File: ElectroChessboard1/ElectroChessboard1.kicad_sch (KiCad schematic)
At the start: 18 parts, among them IC75 DS1307Z+T&R, J2 Conn_01x04_Pin, J3 Conn_01x06, J4 Conn_01x06, SW1 SW_Push, SW2 SW_Push, SW3 SW_Push, SW4 SW_Push, U1 ATmega2560-16A, Y1 Crystal, Y2 XO57CRECNA16M

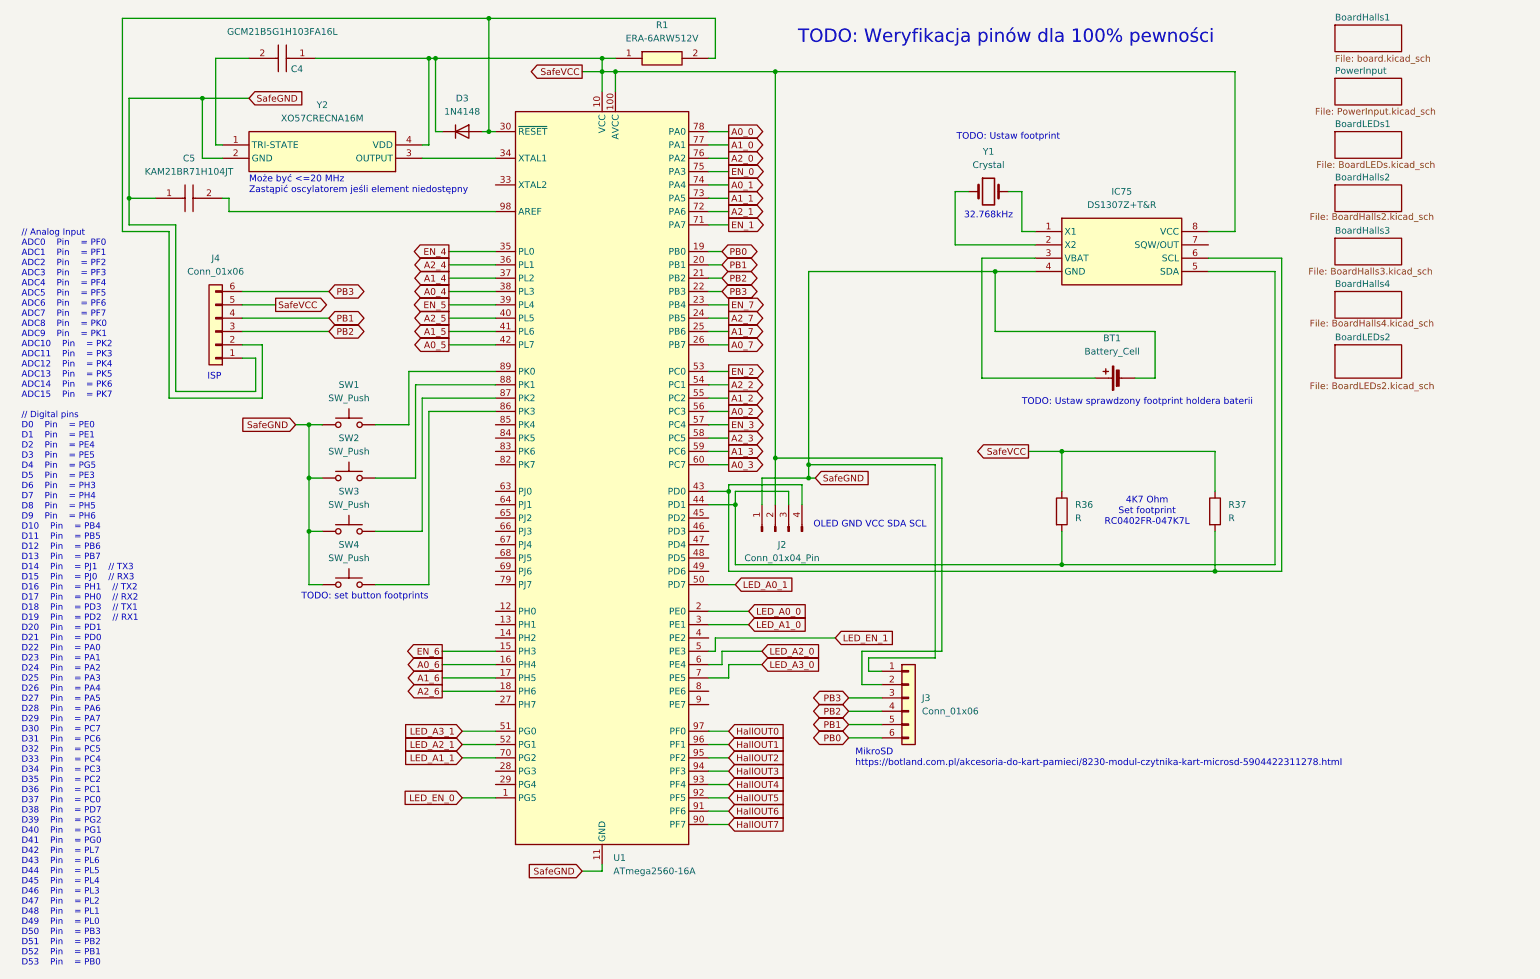
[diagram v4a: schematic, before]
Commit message: Corrected footprints 1
Chosen footprints for JLCPCB
I may add USB insterface chip
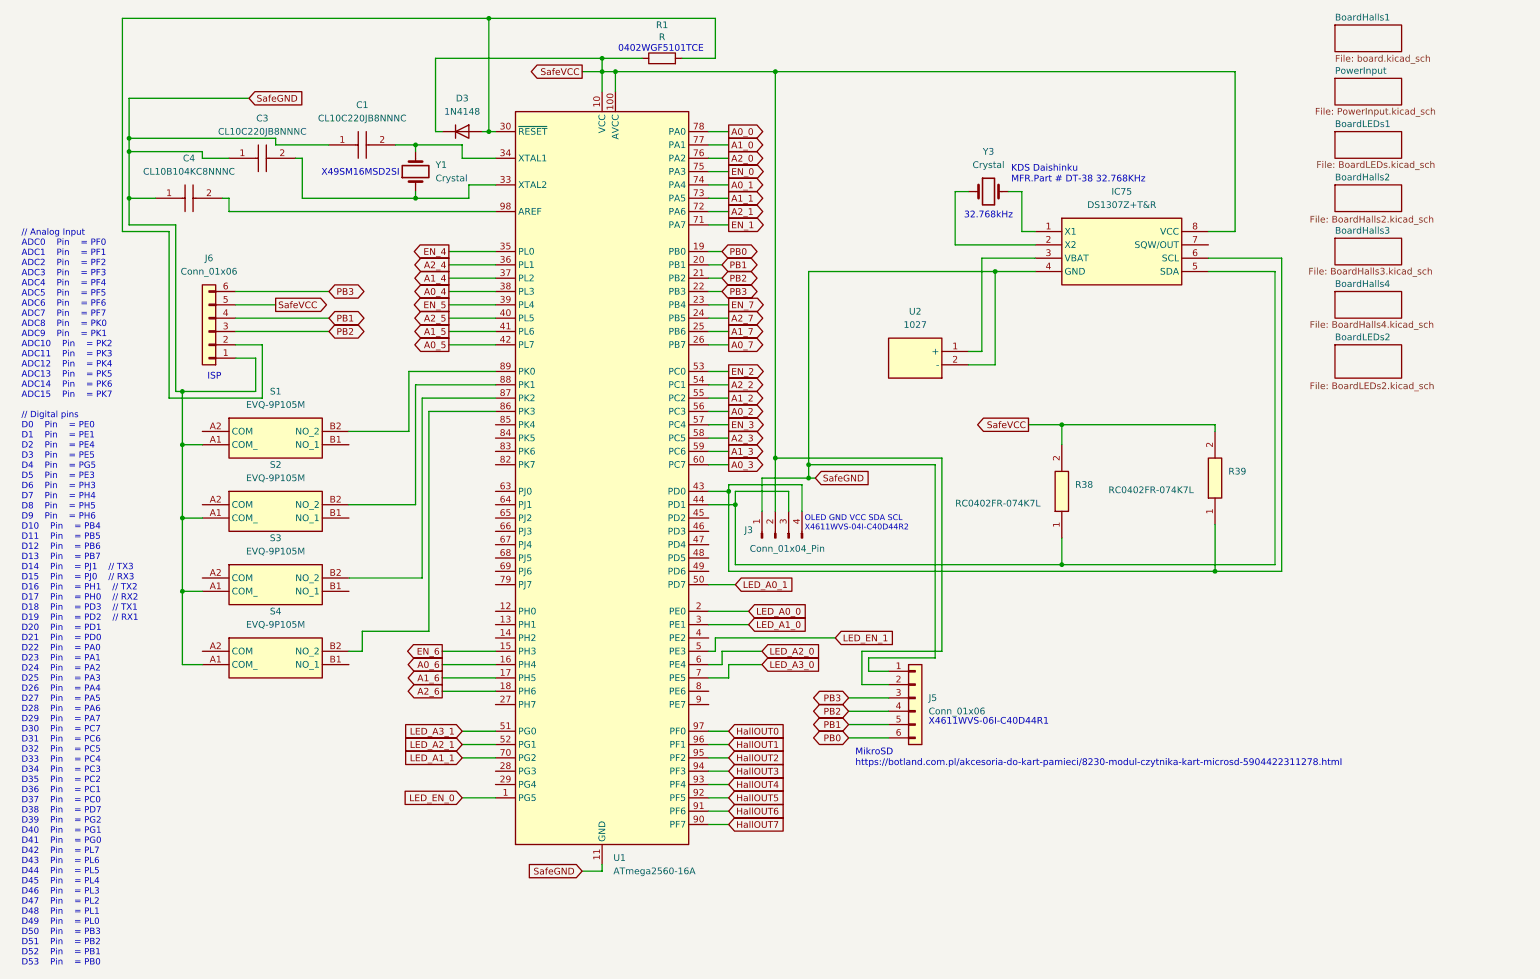
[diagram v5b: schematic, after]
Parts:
- removed BT1: Battery_Cell, symbol Device:Battery_Cell
- removed C4: GCM21B5G1H103FA16L, GCM21, symbol SamacSys_Parts:GCM21B5G1H103FA16L
- removed C5: KAM21BR71H104JT, CAPC2012X94N, symbol SamacSys_Parts:KAM21BR71H104JT
- removed J2: Conn_01x04_Pin, Connector_PinHeader_1.00mm:PinHeader_1x04_P1.00mm_Vertical, symbol Connector:Conn_01x04_Pin
- removed J3, J4: Conn_01x06, Connector_Harwin:Harwin_M20-89006xx_1x06_P2.54mm_Horizontal, symbol Connector_Generic:Conn_01x06
- removed R1: ERA-6ARW512V, ERA6AEB101V, symbol SamacSys_Parts:ERA-6ARW512V
- removed R36, R37: R, symbol Device:R
- removed SW1, SW2, SW3, SW4: SW_Push, symbol Switch:SW_Push
- removed Y2: XO57CRECNA16M, XO57CRECNA16M, symbol SamacSys_Parts:XO57CRECNA16M
- added C1, C3: CL10C220JB8NNNC, SamacSys_Parts:CAPC1608X90N, symbol SamacSys_Parts:CL10C220JB8NNNC
- added C4: CL10B104KC8NNNC, SamacSys_Parts:CAPC1608X90N, symbol SamacSys_Parts:CL10B104KC8NNNC
- added J3: Conn_01x04_Pin, Connector_PinSocket_1.00mm:PinSocket_1x04_P1.00mm_Vertical_SMD_Pin1Left, symbol Connector:Conn_01x04_Pin
- added J5, J6: Conn_01x06, Connector_PinSocket_1.00mm:PinSocket_1x06_P1.00mm_Vertical_SMD_Pin1Right, symbol Connector_Generic:Conn_01x06
- added R1: R, Resistor_SMD:R_0402_1005Metric, symbol Device:R
- added R38, R39: RC0402FR-074K7L, SamacSys_Parts:RESC1005X40N, symbol SamacSys_Parts:RC0402FR-074K7L
- added S1, S2, S3, S4: EVQ-9P105M, SamacSys_Parts:EVQ9P105M, symbol SamacSys_Parts:EVQ-9P105M
- added U2: 1027, SamacSys_Parts:1027, symbol SamacSys_Parts:1027
- added Y3: Crystal, Crystal:Crystal_C38-LF_D3.0mm_L8.0mm_Vertical, symbol Device:Crystal
- D3: footprint Diode_THT:D_DO-35_SOD27_P7.62mm_Horizontal -> Diode_SMD:D_SOD-123
- IC75: footprint SOIC127P600X175-8N -> SamacSys_Parts:SOIC127P600X175-8N
- Y1: footprint (none) -> Crystal:Crystal_SMD_HC49-SD
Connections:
- net PB0: now also J5.6 (Pin_6)
- net PB1: now also J5.5 (Pin_5), J6.4 (Pin_4)
- net PB2: now also J5.4 (Pin_4), J6.3 (Pin_3)
- net PB3: now also J5.3 (Pin_3), J6.6 (Pin_6)
- net SafeGND: now also C1.1, C3.1, C4.1, J3.1 (Pin_1), J5.1 (Pin_1), J6.1 (Pin_1), S1.A1 (COM_), S2.A1 (COM_), S3.A1 (COM_), S4.A1 (COM_), U2.2 (-)
- net SafeVCC: now also J3.2 (Pin_2), J5.2 (Pin_2), J6.5 (Pin_5), R1.1, R38.2, R39.2
- net at IC75.5 (SDA), U1.44 (PD1): now also J3.3 (Pin_3), R38.1
- net at IC75.6 (SCL), U1.43 (PD0): now also J3.4 (Pin_4), R39.1
- net at D3.2 (A), U1.30 (~{RESET}): now also J6.2 (Pin_2), R1.2
- net at U1.33 (XTAL2): now also Y1.1, C3.2
- net at U1.34 (XTAL1): now also Y1.2, C1.2
- net at U1.86 (PK3): now also S4.B2 (NO_2)
- net at U1.87 (PK2): now also S3.B2 (NO_2)
- net at U1.88 (PK1): now also S2.B2 (NO_2)
- net at U1.89 (PK0): now also S1.B2 (NO_2)
- net at U1.98 (AREF): now also C4.2
- net at IC75.1 (X1): now also Y3.2; no longer Y1.2
- net at IC75.2 (X2): now also Y3.1; no longer Y1.1
- net at IC75.3 (VBAT): now also U2.1 (+)
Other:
- note added: "0402WGF5101TCE"
- note added: "KDS Daishinku MFR.Part # DT-38 32.768KHz"
- note added: "OLED GND VCC SDA SCL X4611WVS-04I-C40D44R2"
- note added: "X4611WVS-06I-C40D44R1"
- note added: "X49SM16MSD2SI"
- note removed: "4K7 Ohm Set footprint RC0402FR-047K7L"
- note removed: "Może być <=20 MHz Zastąpić oscylatorem jeśli element niedostępny"
- note removed: "OLED GND VCC SDA SCL"
- note removed: "TODO: Ustaw footprint"
- note removed: "TODO: Ustaw sprawdzony footprint holdera baterii"
- note removed: "TODO: Weryfikacja pinów dla 100% pewności"
- note removed: "TODO: set button footprints"

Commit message: Added FT232RL
Ready for PCB design
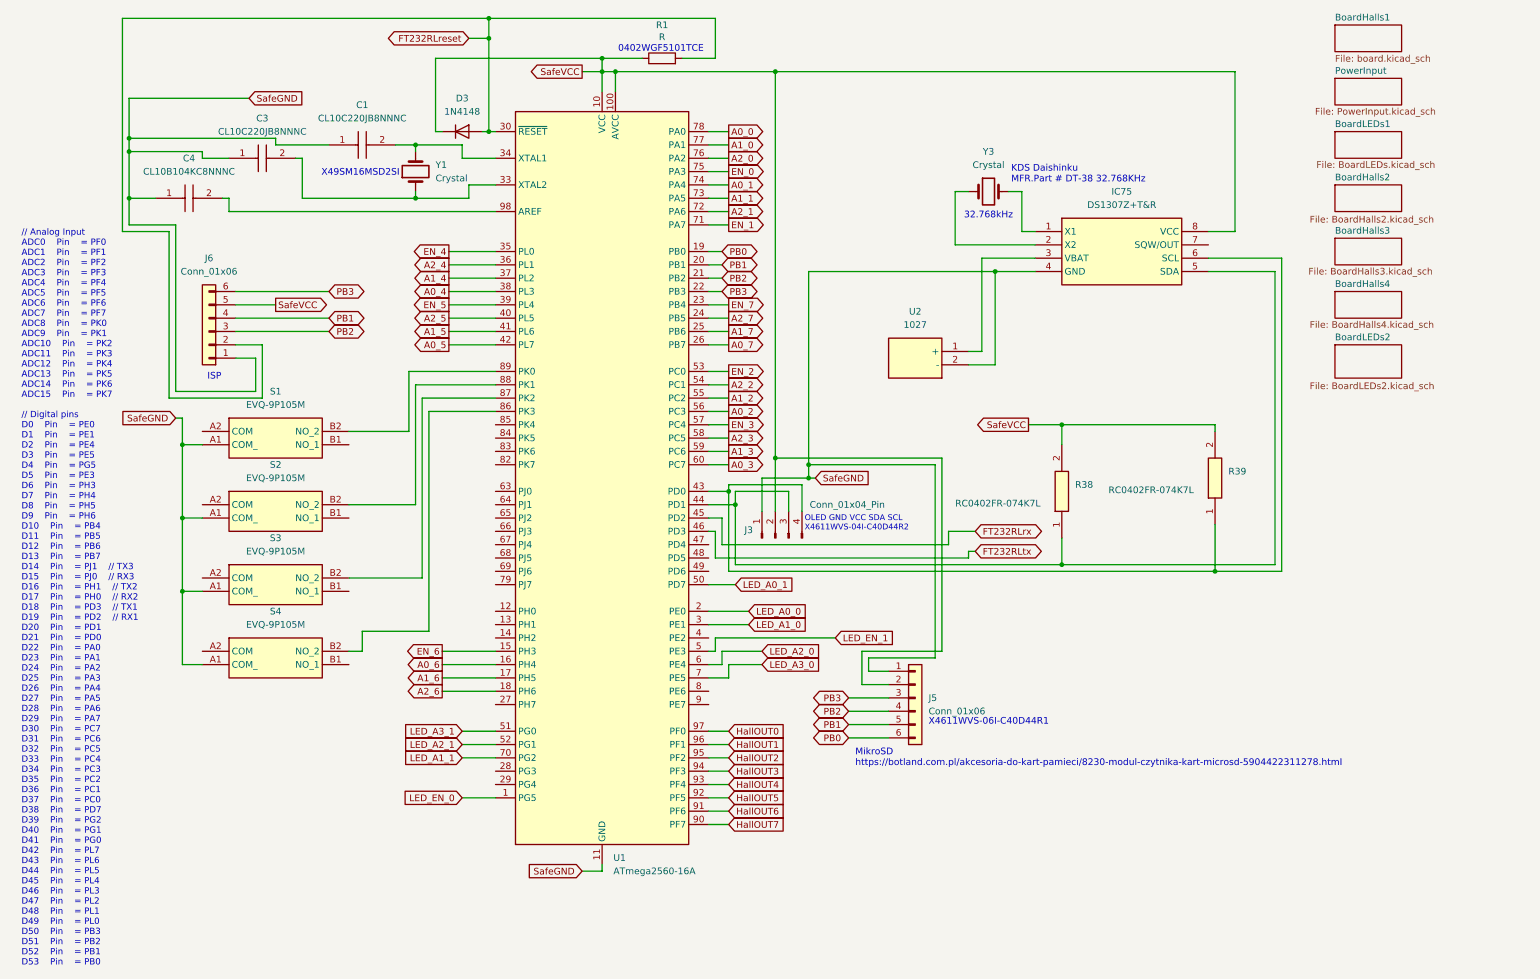
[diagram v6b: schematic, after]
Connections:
- net FT232RLreset: now reaches D3.2 (A), J6.2 (Pin_2), R1.2, U1.30 (~{RESET})
- net FT232RLrx: now reaches U1.45 (PD2)
- net FT232RLtx: now reaches U1.46 (PD3)
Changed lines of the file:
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@@
 	)
 	(junction
+		(at 101.6 17.78)
+		(diameter 0)
+		(color 0 0 0 0)
+	)
+	(junction
+		(at 43.18 95.25)
+		(diameter 0)
+		(color 0 0 0 0)
+	)
+	(junction
 		(at 123.19 24.13)
 		(diameter 0)
@@
 	)
 	(junction
-		(at 43.18 85.09)
-		(diameter 0)
-		(color 0 0 0 0)
-	)
-	(junction
 		(at 125.73 24.13)
 		(diameter 0)
@@
 	)
 	(junction
-		(at 43.18 95.25)
-		(diameter 0)
-		(color 0 0 0 0)
-	)
-	(junction
 		(at 147.32 104.14)
 		(diameter 0)
@@
 	(wire
 		(pts
+			(xy 143.51 111.76) (xy 144.78 111.76)
+		)
+		(stroke
+			(width 0)
+			(type default)
+		)
+	)
+	(wire
+		(pts
 			(xy 195.58 77.47) (xy 193.04 77.47)
 		)
@@
 	(wire
 		(pts
+			(xy 189.23 114.3) (xy 189.23 111.76)
+		)
+		(stroke
+			(width 0)
+			(type default)
+		)
+	)
+	(wire
+		(pts
 			(xy 190.5 46.99) (xy 190.5 57.15)
 		)
@@
 	(wire
 		(pts
+			(xy 144.78 111.76) (xy 144.78 116.84)
+		)
+		(stroke
+			(width 0)
+			(type default)
+		)
+	)
+	(wire
+		(pts
 			(xy 147.32 104.14) (xy 147.32 102.87)
 		)
@@
 	(wire
 		(pts
+			(xy 146.05 109.22) (xy 146.05 114.3)
+		)
+		(stroke
+			(width 0)
+			(type default)
+		)
+	)
+	(wire
+		(pts
 			(xy 143.51 63.5) (xy 146.05 63.5)
 		)
@@
 	(wire
 		(pts
+			(xy 194.31 115.57) (xy 193.04 115.57)
+		)
+		(stroke
+			(width 0)
+			(type default)
+		)
+	)
+	(wire
+		(pts
 			(xy 43.18 137.16) (xy 43.18 123.19)
 		)
@@
 	(wire
 		(pts
-			(xy 123.19 24.13) (xy 123.19 27.94)
-		)
-		(stroke
-			(width 0)
-			(type default)
-		)
-	)
-	(wire
-		(pts
 			(xy 101.6 13.97) (xy 31.75 13.97)
 		)
@@
 	(wire
 		(pts
+			(xy 97.79 17.78) (xy 101.6 17.78)
+		)
+		(stroke
+			(width 0)
+			(type default)
+		)
+	)
+	(wire
+		(pts
 			(xy 93.98 63.5) (xy 102.87 63.5)
 		)
@@
 	(wire
 		(pts
+			(xy 189.23 111.76) (xy 194.31 111.76)
+		)
+		(stroke
+			(width 0)
+			(type default)
+		)
+	)
+	(wire
+		(pts
 			(xy 52.07 48.26) (xy 52.07 50.8)
 		)
@@
 	(wire
 		(pts
+			(xy 41.91 90.17) (xy 43.18 90.17)
+		)
+		(stroke
+			(width 0)
+			(type default)
+		)
+	)
+	(wire
+		(pts
 			(xy 41.91 53.34) (xy 41.91 85.09)
 		)
@@
 	(wire
 		(pts
+			(xy 101.6 17.78) (xy 101.6 35.56)
+		)
+		(stroke
+			(width 0)
+			(type default)
+		)
+	)
+	(wire
+		(pts
 			(xy 143.51 154.94) (xy 147.32 154.94)
 		)
@@
 	(wire
 		(pts
+			(xy 146.05 114.3) (xy 189.23 114.3)
+		)
+		(stroke
+			(width 0)
+			(type default)
+		)
+	)
+	(wire
+		(pts
 			(xy 74.93 106.68) (xy 87.63 106.68)
 		)
@@
 	(wire
 		(pts
-			(xy 101.6 13.97) (xy 101.6 35.56)
+			(xy 101.6 13.97) (xy 101.6 17.78)
 		)
 		(stroke
@@
 	(wire
 		(pts
-			(xy 43.18 85.09) (xy 43.18 95.25)
-		)
-		(stroke
-			(width 0)
-			(type default)
-		)
-	)
-	(wire
-		(pts
 			(xy 156.21 97.79) (xy 156.21 107.95)
 		)
@@
 	(wire
 		(pts
-			(xy 41.91 85.09) (xy 43.18 85.09)
+			(xy 41.91 85.09) (xy 57.15 85.09)
 		)
 		(stroke
@@
 	(wire
 		(pts
-			(xy 170.18 146.05) (xy 177.8 146.05)
+			(xy 144.78 116.84) (xy 193.04 116.84)
 		)
 		(stroke
@@
 	(wire
 		(pts
-			(xy 146.05 134.62) (xy 146.05 137.16)
+			(xy 170.18 146.05) (xy 177.8 146.05)
 		)
 		(stroke
@@
 	(wire
 		(pts
-			(xy 210.82 91.44) (xy 240.03 91.44)
+			(xy 146.05 134.62) (xy 146.05 137.16)
 		)
 		(stroke
@@
 	(wire
 		(pts
-			(xy 60.96 38.1) (xy 60.96 36.83)
+			(xy 210.82 91.44) (xy 240.03 91.44)
 		)
 		(stroke
@@
 	(wire
 		(pts
-			(xy 83.82 38.1) (xy 87.63 38.1)
+			(xy 60.96 38.1) (xy 60.96 36.83)
 		)
 		(stroke
@@
 	(wire
 		(pts
-			(xy 43.18 109.22) (xy 46.99 109.22)
+			(xy 83.82 38.1) (xy 87.63 38.1)
 		)
 		(stroke
@@
 	(wire
 		(pts
-			(xy 144.78 134.62) (xy 144.78 132.08)
+			(xy 43.18 109.22) (xy 46.99 109.22)
 		)
 		(stroke
@@
 	(wire
 		(pts
-			(xy 43.18 85.09) (xy 57.15 85.09)
+			(xy 144.78 134.62) (xy 144.78 132.08)
 		)
 		(stroke
@@
 	(wire
 		(pts
+			(xy 123.19 24.13) (xy 123.19 27.94)
+		)
+		(stroke
+			(width 0)
+			(type default)
+		)
+	)
+	(wire
+		(pts
 			(xy 146.05 137.16) (xy 143.51 137.16)
 		)
@@
 	(wire
 		(pts
+			(xy 193.04 115.57) (xy 193.04 116.84)
+		)
+		(stroke
+			(width 0)
+			(type default)
+		)
+	)
+	(wire
+		(pts
 			(xy 100.33 35.56) (xy 101.6 35.56)
 		)
@@
 	(wire
 		(pts
+			(xy 43.18 90.17) (xy 43.18 95.25)
+		)
+		(stroke
+			(width 0)
+			(type default)
+		)
+	)
+	(wire
+		(pts
 			(xy 143.51 134.62) (xy 144.78 134.62)
 		)
@@
 	(wire
 		(pts
+			(xy 143.51 109.22) (xy 146.05 109.22)
+		)
+		(stroke
+			(width 0)
+			(type default)
+		)
+	)
+	(wire
+		(pts
 			(xy 143.51 121.92) (xy 148.59 121.92)
 		)
@@
 		)
 	)
+	(global_label "FT232RLtx"
+		(shape bidirectional)
+		(at 194.31 115.57 0)
+		(fields_autoplaced yes)
+		(effects
+			(font
+				(size 1.27 1.27)
+			)
+			(justify left)
+		)
+		(property "Intersheetrefs" "${INTERSHEET_REFS}"
+			(at 208.1431 115.57 0)
+			(effects
+				(font
+					(size 1.27 1.27)
+				)
+				(justify left)
+				(hide yes)
+			)
+		)
+	)
 	(global_label "PB1"
 		(shape bidirectional)
@@
 		)
 	)
+	(global_label "SafeGND"
+		(shape input)
+		(at 41.91 90.17 180)
+		(fields_autoplaced yes)
+		(effects
+			(font
+				(size 1.27 1.27)
+				(color 55 126 255 1)
+			)
+			(justify right)
+		)
+		(property "Intersheetrefs" "${INTERSHEET_REFS}"
+			(at 30.8815 90.17 0)
+			(effects
+				(font
+					(size 1.27 1.27)
+				)
+				(justify right)
+				(hide yes)
+			)
+		)
+	)
 	(global_label "PB3"
 		(shape bidirectional)
@@
 		)
 	)
+	(global_label "FT232RLrx"
+		(shape bidirectional)
+		(at 194.31 111.76 0)
+		(fields_autoplaced yes)
+		(effects
+			(font
+				(size 1.27 1.27)
+			)
+			(justify left)
+		)
+		(property "Intersheetrefs" "${INTERSHEET_REFS}"
+			(at 208.2036 111.76 0)
+			(effects
+				(font
+					(size 1.27 1.27)
+				)
+				(justify left)
+				(hide yes)
+			)
+		)
+	)
 	(global_label "A1_3"
 		(shape output)
@@
 		)
 	)
+	(global_label "FT232RLreset"
+		(shape bidirectional)
+		(at 97.79 17.78 180)
+		(fields_autoplaced yes)
+		(effects
+			(font
+				(size 1.27 1.27)
+			)
+			(justify right)
+		)
+		(property "Intersheetrefs" "${INTERSHEET_REFS}"
+			(at 80.9935 17.78 0)
+			(effects
+				(font
+					(size 1.27 1.27)
+				)
+				(justify right)
+				(hide yes)
+			)
+		)
+	)
 	(global_label "HallOUT2"
 		(shape input)
@@
 		)
 		(property "Value" "Conn_01x04_Pin"
-			(at 158.496 115.062 90)
+			(at 169.926 106.68 90)
 			(effects
 				(font

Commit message: update
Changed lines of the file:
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@@
 	(wire
 		(pts
-			(xy 102.87 83.82) (xy 87.63 83.82)
+			(xy 102.87 83.82) (xy 77.47 83.82)
 		)
 		(stroke
@@
 	(wire
 		(pts
-			(xy 86.36 81.28) (xy 86.36 92.71)
+			(xy 76.2 81.28) (xy 76.2 92.71)
 		)
 		(stroke
@@
 	(wire
 		(pts
-			(xy 88.9 120.65) (xy 88.9 86.36)
+			(xy 78.74 120.65) (xy 78.74 86.36)
 		)
 		(stroke
@@
 	(wire
 		(pts
-			(xy 74.93 120.65) (xy 88.9 120.65)
+			(xy 74.93 120.65) (xy 78.74 120.65)
 		)
 		(stroke
@@
 	(wire
 		(pts
-			(xy 77.47 130.81) (xy 90.17 130.81)
+			(xy 77.47 130.81) (xy 80.01 130.81)
 		)
 		(stroke
@@
 	(wire
 		(pts
-			(xy 102.87 81.28) (xy 86.36 81.28)
+			(xy 102.87 81.28) (xy 76.2 81.28)
 		)
 		(stroke
@@
 	(wire
 		(pts
-			(xy 87.63 83.82) (xy 87.63 106.68)
+			(xy 77.47 83.82) (xy 77.47 106.68)
 		)
 		(stroke
@@
 	(wire
 		(pts
-			(xy 90.17 88.9) (xy 102.87 88.9)
+			(xy 80.01 88.9) (xy 102.87 88.9)
 		)
 		(stroke
@@
 	(wire
 		(pts
-			(xy 90.17 130.81) (xy 90.17 88.9)
+			(xy 80.01 130.81) (xy 80.01 88.9)
 		)
 		(stroke
@@
 	(wire
 		(pts
-			(xy 74.93 106.68) (xy 87.63 106.68)
+			(xy 74.93 106.68) (xy 77.47 106.68)
 		)
 		(stroke
@@
 	(wire
 		(pts
-			(xy 74.93 92.71) (xy 86.36 92.71)
+			(xy 74.93 92.71) (xy 76.2 92.71)
 		)
 		(stroke
@@
 	(wire
 		(pts
-			(xy 88.9 86.36) (xy 102.87 86.36)
-		)
-		(stroke
+			(xy 78.74 86.36) (xy 102.87 86.36)
+		)
+		(stroke
